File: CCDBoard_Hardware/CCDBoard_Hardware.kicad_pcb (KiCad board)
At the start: 2 copper layers, 63.5 x 38.1 mm, 30 parts, among them U1 S11639-01, U2 LT1818, U3 74HC541

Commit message: improvements that might break things
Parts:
- moved TP1 29.7 mm to (141.2, 85.1)
- moved C8 28.0 mm to (144.9, 87.9)
- moved R4 28.0 mm to (144.9, 89.7)
- moved U2 27.5 mm to (146.9, 93.4)
- moved C7 26.5 mm to (142.0, 93.7)
- moved C2 24.9 mm to (144.0, 93.9), turned to 90 degrees
- moved Conn2 23.2 mm to (129.7, 80.6), turned to 180 degrees
- moved TP5 14.7 mm to (112.0, 87.1)
- moved R1 13.7 mm to (138.2, 90.5), turned to 90 degrees
- moved Conn1 11.4 mm to (106.2, 86.4)
- moved TP2 10.1 mm to (121.4, 78.2)
- moved C6 8.23 mm to (121.9, 85.5), turned to 90 degrees
- moved C5 8.21 mm to (119.9, 95.9), turned to 90 degrees
- moved C10 8.02 mm to (119.9, 85.3), turned to 90 degrees
- moved R2 7.87 mm to (121.9, 89.5)
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- renumbered Video to TP1, Trig to TP2, EOS to TP3, PreAmpVid to TP4, CLK to TP5, ST to TP6
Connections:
- Conn1 pad 2: ST -> CLK
- Conn1 pad 3: CLK -> ST
- Conn2 pad 1: Trig -> Video
- Conn2 pad 3: Video -> Trig
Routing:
- net Net-(R3-Pad1): track 36.0 -> 3.97 mm, vias 2 -> 0
- net EOS: track 34.8 -> 15.9 mm, vias 1 -> 0
- net Trig: track 32.6 -> 14.1 mm, vias 1 -> 0
- net Net-(R1-Pad1): track 36.7 -> 23.7 mm
- net Trig_OUT: track 16.4 -> 5.69 mm, vias 2 -> 0
- net +5V: track 27.2 -> 37.5 mm, vias 2 -> 1
- net ST_IN: track 16.4 -> 6.44 mm, vias 2 -> 0
- net ST: track 35.7 -> 26.0 mm
- net CLK_IN: track 3.40 -> 12.2 mm
- net CLK: track 35.9 -> 28.0 mm, vias 3 -> 1
- net Net-(C5-Pad1): track 3.96 -> 11.6 mm
- net Net-(R2-Pad2): track 16.0 -> 8.79 mm, vias 2 -> 0
- net Net-(R3-Pad2): track 11.3 -> 6.75 mm, vias 1 -> 0
- net EOS_OUT: track 14.9 -> 17.6 mm
- net Video: track 16.3 -> 18.4 mm
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
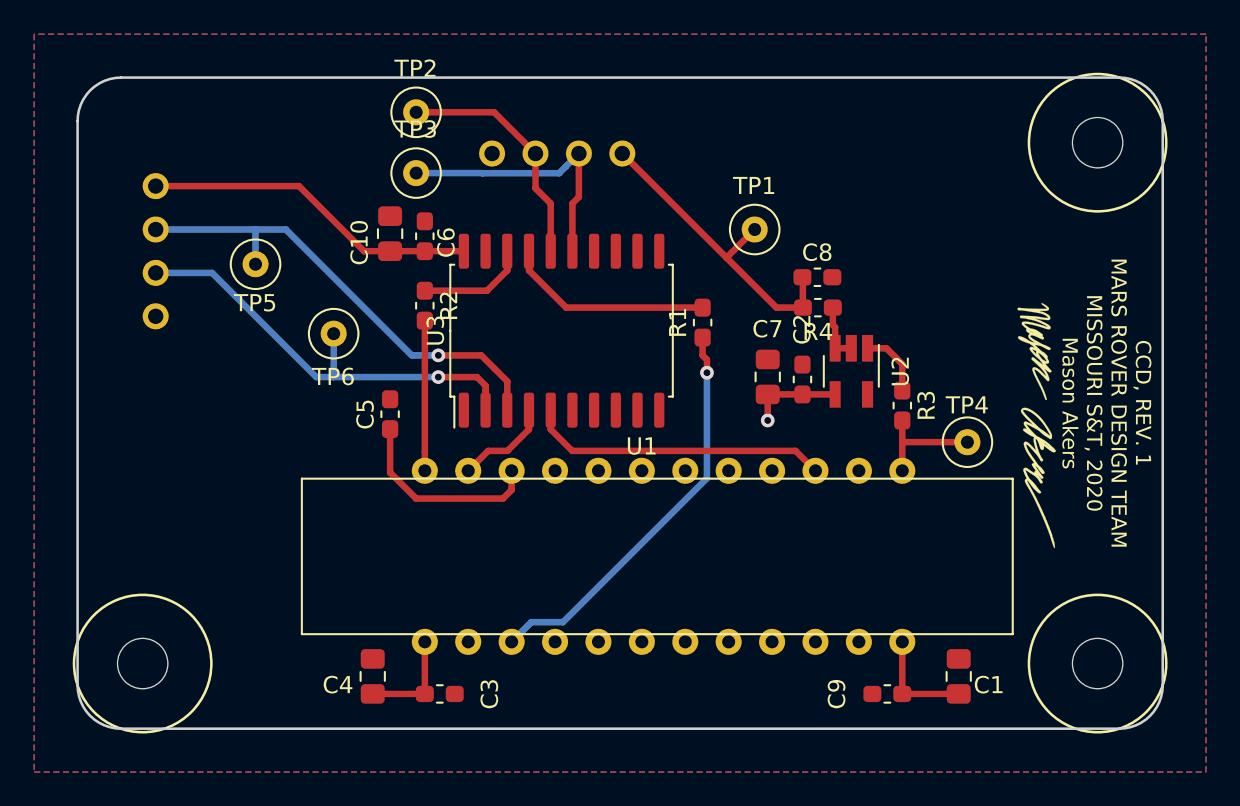
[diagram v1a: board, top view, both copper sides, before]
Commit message: Revert "improvements that might break things"
This reverts commit 929e755a3a655d7aa2cd30a99533c48bf9da1e19.
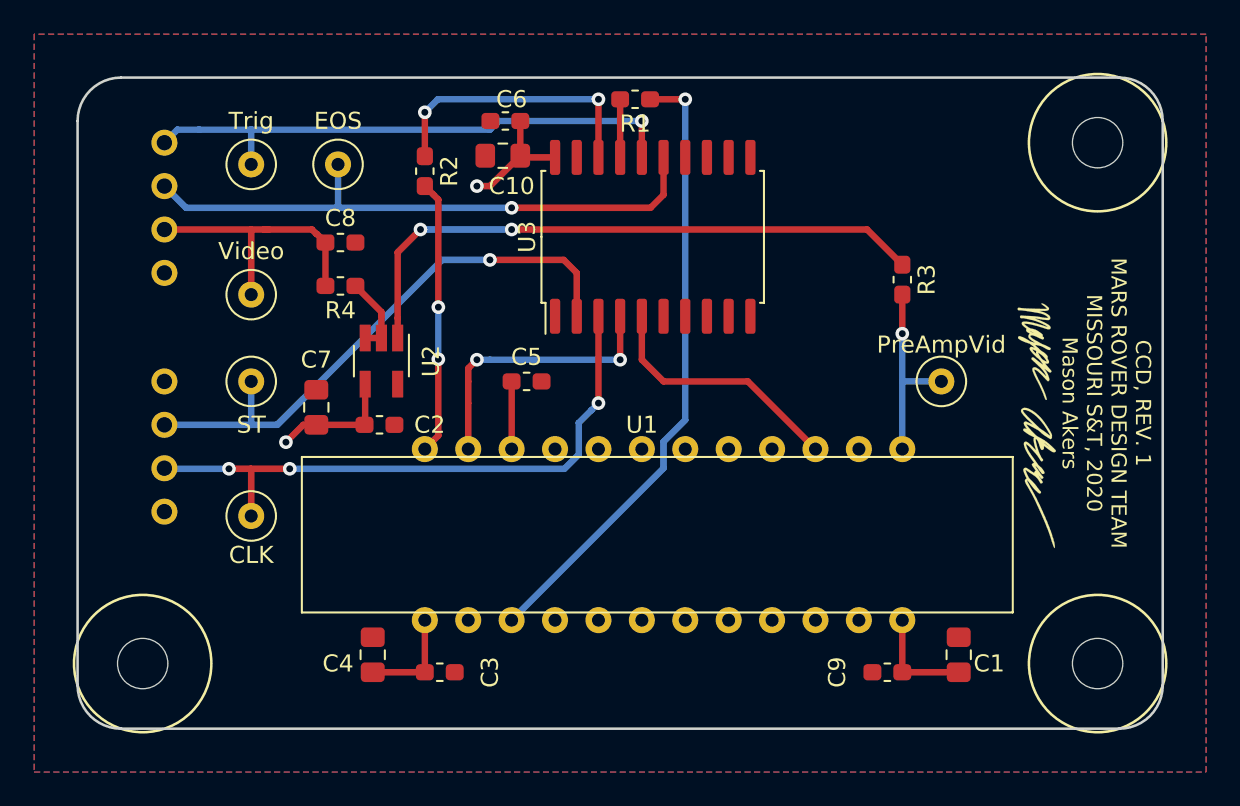
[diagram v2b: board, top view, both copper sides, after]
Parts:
- moved Video 29.7 mm to (111.8, 88.9)
- moved C8 28.0 mm to (117.0, 85.9)
- moved R4 28.0 mm to (117.0, 88.4)
- moved U2 27.5 mm to (119.4, 92.8)
- moved C7 26.5 mm to (115.6, 95.5)
- moved C2 24.9 mm to (119.3, 96.5), turned to 0 degrees
- moved Conn2 23.2 mm to (106.7, 83.8), turned to 270 degrees
- moved CLK 14.7 mm to (111.8, 101.9)
- moved R1 13.7 mm to (134.2, 77.5), turned to 180 degrees
- moved Conn1 11.4 mm to (106.7, 97.8)
- moved Trig 10.1 mm to (111.8, 81.3)
- moved C6 8.23 mm to (126.6, 78.7), turned to 180 degrees
- moved C5 8.21 mm to (127.9, 94.0), turned to 0 degrees
- moved C10 8.02 mm to (126.5, 80.8), turned to 180 degrees
- moved R2 7.87 mm to (121.9, 81.7)
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- renumbered TP5 to CLK, TP3 to EOS, TP4 to PreAmpVid, TP6 to ST, TP2 to Trig, TP1 to Video
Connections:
- Conn1 pad 2: CLK -> ST
- Conn1 pad 3: ST -> CLK
- Conn2 pad 1: Video -> Trig
- Conn2 pad 3: Trig -> Video
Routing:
- net Net-(R3-Pad1): track 3.97 -> 36.0 mm, vias 0 -> 2
- net EOS: track 15.9 -> 34.8 mm, vias 0 -> 1
- net Trig: track 14.1 -> 32.6 mm, vias 0 -> 1
- net Net-(R1-Pad1): track 23.7 -> 36.7 mm
- net Trig_OUT: track 5.69 -> 16.4 mm, vias 0 -> 2
- net +5V: track 37.5 -> 27.2 mm, vias 1 -> 2
- net ST_IN: track 6.44 -> 16.4 mm, vias 0 -> 2
- net ST: track 26.0 -> 35.7 mm
- net CLK_IN: track 12.2 -> 3.40 mm
- net CLK: track 28.0 -> 35.9 mm, vias 1 -> 3
- net Net-(C5-Pad1): track 11.6 -> 3.96 mm
- net Net-(R2-Pad2): track 8.79 -> 16.0 mm, vias 0 -> 2
- net Net-(R3-Pad2): track 6.75 -> 11.3 mm, vias 0 -> 1
- net EOS_OUT: track 17.6 -> 14.9 mm
- net Video: track 18.4 -> 16.3 mm
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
